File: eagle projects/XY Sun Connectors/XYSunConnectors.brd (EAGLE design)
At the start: 25 x 67 mm, 2 parts, among them J1 FPC_HIROSE_FH19C-6S-0.5SH(10)

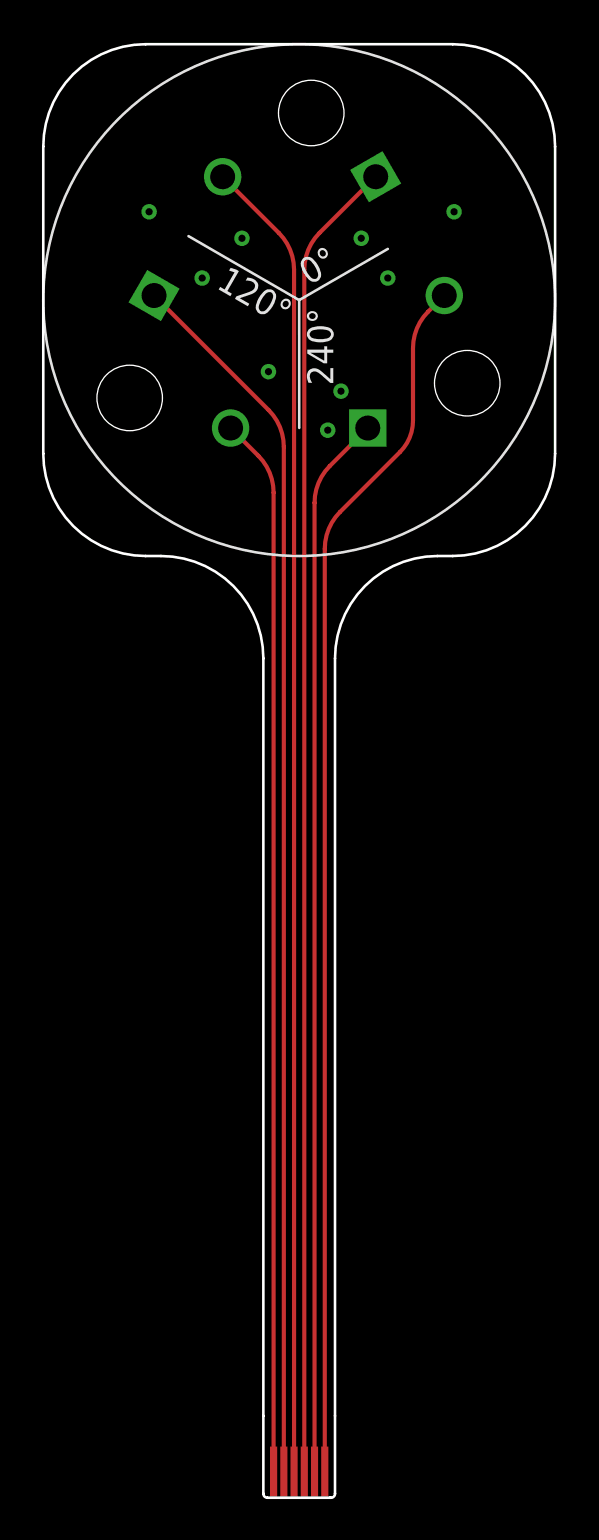
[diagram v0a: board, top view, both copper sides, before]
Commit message: Updated XY Sun Sensor Board
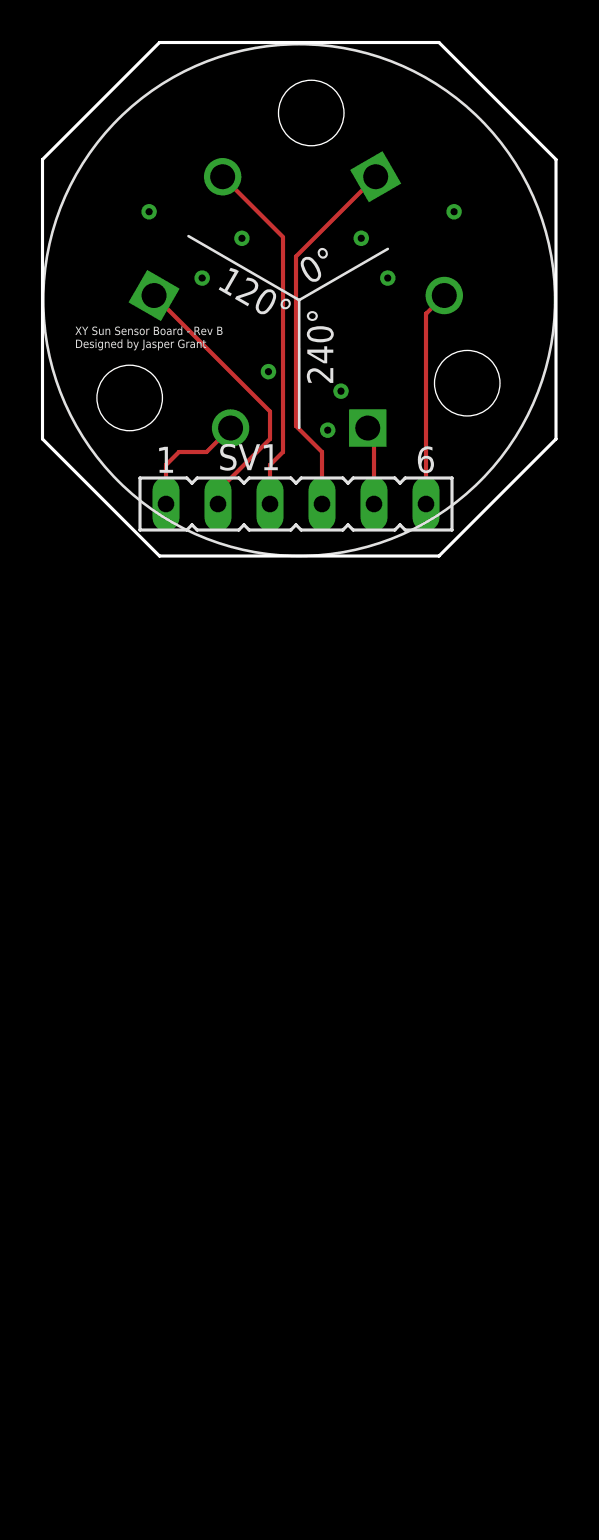
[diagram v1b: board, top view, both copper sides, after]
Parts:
- removed J1: FPC_HIROSE_FH19C-6S-0.5SH(10), my_library:FPC_HIROSE_FH19C-6S-0.5SH(10)
- added SV1: (no value), con-lsta:FE06
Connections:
- net A1: now also SV1.6; no longer J1.6
- net A2: now also SV1.3; no longer J1.3
- net A3: now also SV1.1; no longer J1.1
- net C1: now also SV1.4; no longer J1.4
- net C2: now also SV1.2; no longer J1.2
- net C3: now also SV1.5; no longer J1.5
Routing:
- net A1: track 59.4 -> 10.6 mm
- net C3: track 51.9 -> 3.84 mm
- net A2: track 64.6 -> 17.5 mm
- net C1: track 64.6 -> 18.1 mm
- net C2: track 59.9 -> 13.6 mm
- net A3: track 52.6 -> 6.44 mm
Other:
- board size 25 x 67 mm -> 25.1 x 25.1 mm
- board text added: "Designed by Jasper Grant"
- board text added: "XY Sun Sensor Board - Rev B"
- board text removed: "STIFFENER FR4"
- board text removed: "STIFFENER PI"
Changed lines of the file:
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@@
 <setting verticaltext="up"/>
 </settings>
-<grid distance="25" unitdist="mil" unit="mil" style="lines" multiple="1" display="no" altdistance="12" altunitdist="mil" altunit="mil"/>
+<grid distance="12.5" unitdist="mil" unit="mil" style="lines" multiple="1" display="no" altdistance="12" altunitdist="mil" altunit="mil"/>
 <layers>
 <layer number="1" name="Top" color="4" fill="1" visible="yes" active="yes"/>
@@
 <board>
 <plain>
-<wire x1="17.5" y1="68.5" x2="17.5" y2="83.5" width="0.127" layer="20"/>
-<wire x1="17.5" y1="83.5" x2="22.5" y2="88.5" width="0.127" layer="20" curve="-90"/>
-<wire x1="22.5" y1="88.5" x2="37.5" y2="88.5" width="0.127" layer="20"/>
-<wire x1="37.5" y1="88.5" x2="42.5" y2="83.5" width="0.127" layer="20" curve="-90"/>
-<wire x1="42.5" y1="83.5" x2="42.5" y2="68.5" width="0.127" layer="20"/>
-<wire x1="42.5" y1="68.5" x2="37.5" y2="63.5" width="0.127" layer="20" curve="-90"/>
-<wire x1="37.5" y1="63.5" x2="36.75" y2="63.5" width="0.127" layer="20"/>
-<wire x1="36.75" y1="63.5" x2="31.75" y2="58.5" width="0.127" layer="20" curve="90"/>
-<wire x1="31.75" y1="58.5" x2="31.75" y2="21.5" width="0.127" layer="20"/>
-<wire x1="28.25" y1="21.5" x2="28.25" y2="58.5" width="0.127" layer="20"/>
-<wire x1="28.25" y1="58.5" x2="23.25" y2="63.5" width="0.127" layer="20" curve="90"/>
-<wire x1="23.25" y1="63.5" x2="22.5" y2="63.5" width="0.127" layer="20"/>
-<wire x1="22.5" y1="63.5" x2="17.5" y2="68.5" width="0.127" layer="20" curve="-90"/>
-<dimension x1="37.5" y1="88.5" x2="37.5" y2="63.5" x3="50.8" y3="76" textsize="1.778" layer="115"/>
-<text x="53.975" y="66.04" size="1.778" layer="115" rot="R90">STIFFENER FR4</text>
-<text x="10.795" y="18.415" size="1.778" layer="114">STIFFENER PI</text>
+<wire x1="23.1775" y1="63.5" x2="36.83" y2="63.5" width="0.1524" layer="20"/>
+<wire x1="23.1775" y1="63.5" x2="17.4625" y2="69.215" width="0.1524" layer="20"/>
+<wire x1="36.83" y1="63.5" x2="42.545" y2="69.215" width="0.1524" layer="20"/>
+<wire x1="17.4625" y1="69.215" x2="17.4625" y2="82.8675" width="0.1524" layer="20"/>
+<wire x1="17.4625" y1="82.8675" x2="23.1775" y2="88.5825" width="0.1524" layer="20"/>
+<wire x1="23.1775" y1="88.5825" x2="36.83" y2="88.5825" width="0.1524" layer="20"/>
+<wire x1="36.83" y1="88.5825" x2="42.545" y2="82.8675" width="0.1524" layer="20"/>
+<wire x1="42.545" y1="82.8675" x2="42.545" y2="69.215" width="0.1524" layer="20"/>
+<text x="19.05" y="74.295" size="0.4064" layer="25">XY Sun Sensor Board - Rev B</text>
+<text x="19.05" y="73.66" size="0.4064" layer="25">Designed by Jasper Grant</text>
 </plain>
 <attributes>
@@
 </autorouter>
 <elements>
-<element name="J1" library="my_library" library_urn="urn:adsk.eagle:library:22876504" package="FPC_HIROSE_FH19C-6S-0.5SH(10)" value="FPC_HIROSE_FH19C-6S-0.5SH(10)" x="30" y="20" smashed="yes" rot="R180"/>
 <element name="A2" library="my_library" library_urn="urn:adsk.eagle:library:22876504" package="XY_SUN_SENOR_MASK" value="XY_SUN_SENSOR" x="30" y="76" smashed="yes" rot="R30"/>
+<element name="SV1" library="con-lsta" library_urn="urn:adsk.eagle:library:161" package="FE06" package3d_urn="urn:adsk.eagle:package:8191/1" value="" x="29.845" y="66.04" smashed="yes">
+<attribute name="MF" value="" x="29.845" y="66.04" size="1.778" layer="27" display="off"/>
+<attribute name="MPN" value="" x="29.845" y="66.04" size="1.778" layer="27" display="off"/>
+<attribute name="NAME" x="26.035" y="67.691" size="1.27" layer="25" ratio="10"/>
+<attribute name="OC_FARNELL" value="unknown" x="29.845" y="66.04" size="1.778" layer="27" display="off"/>
+<attribute name="OC_NEWARK" value="unknown" x="29.845" y="66.04" size="1.778" layer="27" display="off"/>
+<attribute name="POPULARITY" value="11" x="29.845" y="66.04" size="1.778" layer="27" display="off"/>
+<attribute name="VALUE" x="22.225" y="63.119" size="1.27" layer="27" ratio="10"/>
+</element>
 </elements>
 <signals>
 <signal name="A3">
-<contactref element="J1" pad="1"/>
-<wire x1="28.75" y1="19.685" x2="28.75" y2="18.75" width="0.1524" layer="1"/>
-<wire x1="28.75" y1="18.75" x2="28.75" y2="66.59789375" width="0.2032" layer="1"/>
-<wire x1="28.75" y1="66.59789375" x2="28.00605" y2="68.393946875" width="0.2032" layer="1" curve="45"/>
 <contactref element="A2" pad="A3"/>
-<wire x1="28.00605" y1="68.393946875" x2="26.65" y2="69.749996875" width="0.2032" layer="1"/>
+<contactref element="SV1" pad="1"/>
+<wire x1="23.495" y1="65.405" x2="23.495" y2="66.04" width="0" layer="19" extent="1-1"/>
+<wire x1="26.65" y1="69.749996875" x2="25.480003125" y2="68.58" width="0.2032" layer="1"/>
+<wire x1="25.480003125" y1="68.58" x2="24.13" y2="68.58" width="0.2032" layer="1"/>
+<wire x1="24.13" y1="68.58" x2="23.495" y2="67.945" width="0.2032" layer="1"/>
+<wire x1="23.495" y1="67.945" x2="23.495" y2="65.405" width="0.2032" layer="1"/>
 </signal>
 <signal name="C3">
-<contactref element="J1" pad="5"/>
-<wire x1="30.75" y1="18.75" x2="30.75" y2="66.097896875" width="0.2032" layer="1"/>
-<wire x1="30.75" y1="66.097896875" x2="31.49395" y2="67.89395" width="0.2032" layer="1" curve="-45"/>
 <contactref element="A2" pad="C3"/>
-<wire x1="31.49395" y1="67.89395" x2="33.349996875" y2="69.749996875" width="0.2032" layer="1"/>
+<contactref element="SV1" pad="5"/>
+<wire x1="33.655" y1="69.44499375" x2="33.349996875" y2="69.749996875" width="0.2032" layer="1"/>
+<wire x1="33.655" y1="66.04" x2="33.655" y2="69.44499375" width="0.2032" layer="1"/>
 </signal>
 <signal name="C2">
-<contactref element="J1" pad="2"/>
-<wire x1="29.25" y1="68.834053125" x2="28.50605" y2="70.63010625" width="0.2032" layer="1" curve="45"/>
-<wire x1="29.25" y1="68.834053125" x2="29.25" y2="18.75" width="0.2032" layer="1"/>
 <contactref element="A2" pad="C2"/>
-<wire x1="28.50605" y1="70.63010625" x2="22.912340625" y2="76.223815625" width="0.2032" layer="1"/>
+<contactref element="SV1" pad="2"/>
+<wire x1="26.035" y1="66.04" x2="26.035" y2="66.675" width="0.2032" layer="1"/>
+<wire x1="26.035" y1="66.675" x2="28.575" y2="69.215" width="0.2032" layer="1"/>
+<wire x1="22.912340625" y1="76.223815625" x2="28.575" y2="70.56115625" width="0.2032" layer="1"/>
+<wire x1="28.575" y1="70.56115625" x2="28.575" y2="69.215" width="0.2032" layer="1"/>
 </signal>
 <signal name="N$7">
@@
 </signal>
 <signal name="C1">
-<contactref element="J1" pad="4"/>
 <contactref element="A2" pad="C1"/>
-<wire x1="30.25" y1="18.75" x2="30.25" y2="77.486425" width="0.2032" layer="1"/>
-<wire x1="30.25" y1="77.486425" x2="30.99395" y2="79.282478125" width="0.2032" layer="1" curve="-45"/>
-<wire x1="30.99395" y1="79.282478125" x2="33.73765625" y2="82.026184375" width="0.2032" layer="1"/>
+<contactref element="SV1" pad="4"/>
+<wire x1="31.115" y1="66.04" x2="31.115" y2="68.58" width="0.2032" layer="1"/>
+<wire x1="31.115" y1="68.58" x2="29.845" y2="69.85" width="0.2032" layer="1"/>
+<wire x1="29.845" y1="69.85" x2="29.845" y2="78.133528125" width="0.2032" layer="1"/>
+<wire x1="29.845" y1="78.133528125" x2="33.73765625" y2="82.026184375" width="0.2032" layer="1"/>
 </signal>
 <signal name="A2">
-<contactref element="J1" pad="3"/>
 <contactref element="A2" pad="A2"/>
-<wire x1="26.2623375" y1="82.026184375" x2="29.00605" y2="79.282471875" width="0.2032" layer="1"/>
-<wire x1="29.00605" y1="79.282471875" x2="29.75" y2="77.48641875" width="0.2032" layer="1" curve="-45"/>
-<wire x1="29.75" y1="77.48641875" x2="29.75" y2="18.75" width="0.2032" layer="1"/>
+<contactref element="SV1" pad="3"/>
+<wire x1="28.575" y1="66.04" x2="28.575" y2="67.945" width="0.2032" layer="1"/>
+<wire x1="28.575" y1="67.945" x2="29.21" y2="68.58" width="0.2032" layer="1"/>
+<wire x1="29.21" y1="79.078521875" x2="26.2623375" y2="82.026184375" width="0.2032" layer="1"/>
+<wire x1="29.21" y1="68.58" x2="29.21" y2="79.078521875" width="0.2032" layer="1"/>
 </signal>
 <signal name="A1">
-<contactref element="J1" pad="6"/>
 <contactref element="A2" pad="A1"/>
-<wire x1="31.25" y1="18.75" x2="31.25" y2="63.852896875" width="0.2032" layer="1"/>
-<wire x1="31.25" y1="63.852896875" x2="31.99395" y2="65.64895" width="0.2032" layer="1" curve="-45"/>
-<wire x1="31.99395" y1="65.64895" x2="34.925" y2="68.58" width="0.2032" layer="1"/>
-<wire x1="34.925" y1="68.58" x2="35.56" y2="70.113025" width="0.2032" layer="1" curve="45"/>
-<wire x1="35.56" y1="70.113025" x2="35.56" y2="73.66" width="0.2032" layer="1"/>
-<wire x1="35.56" y1="73.66" x2="36.292671875" y2="75.428828125" width="0.2032" layer="1" curve="-45"/>
-<wire x1="36.292671875" y1="75.428828125" x2="37.08765625" y2="76.2238125" width="0.2032" layer="1"/>
+<contactref element="SV1" pad="6"/>
+<wire x1="36.195" y1="66.04" x2="36.195" y2="75.33115625" width="0.2032" layer="1"/>
+<wire x1="36.195" y1="75.33115625" x2="37.08765625" y2="76.2238125" width="0.2032" layer="1"/>
 </signal>
 </signals>
@@
 with this version.
 </note>
+<note version="8.3" severity="warning">
+Since Version 8.3, EAGLE supports URNs for individual library
+assets (packages, symbols, and devices). The URNs of those assets
+will not be understood (or retained) with this version.
+</note>
+<note version="8.3" severity="warning">
+Since Version 8.3, EAGLE supports the association of 3D packages
+with devices in libraries, schematics, and board files. Those 3D
+packages will not be understood (or retained) with this version.
+</note>
 </compatibility>
